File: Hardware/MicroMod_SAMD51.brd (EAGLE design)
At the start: 22 x 22 mm, 36 parts, among them J2 MICROMOD-2222, U1 W25QXX128MBIT-6X5-NO_CENTER, U2 ATSAMD51J20A-A, Y1 32.768kHz

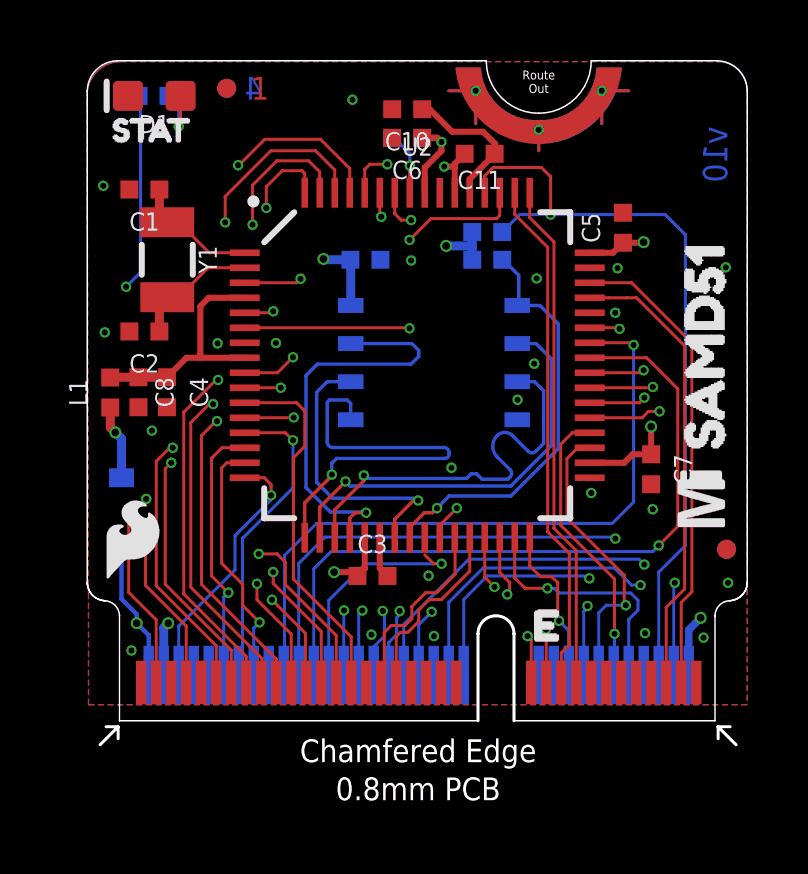
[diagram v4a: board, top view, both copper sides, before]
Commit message: Various testing elements in Variant files regarding Serial1 and Serial2
* Changes old SPI naming convention to new one
* Moves some pins around for more thought out layout (more details to come)
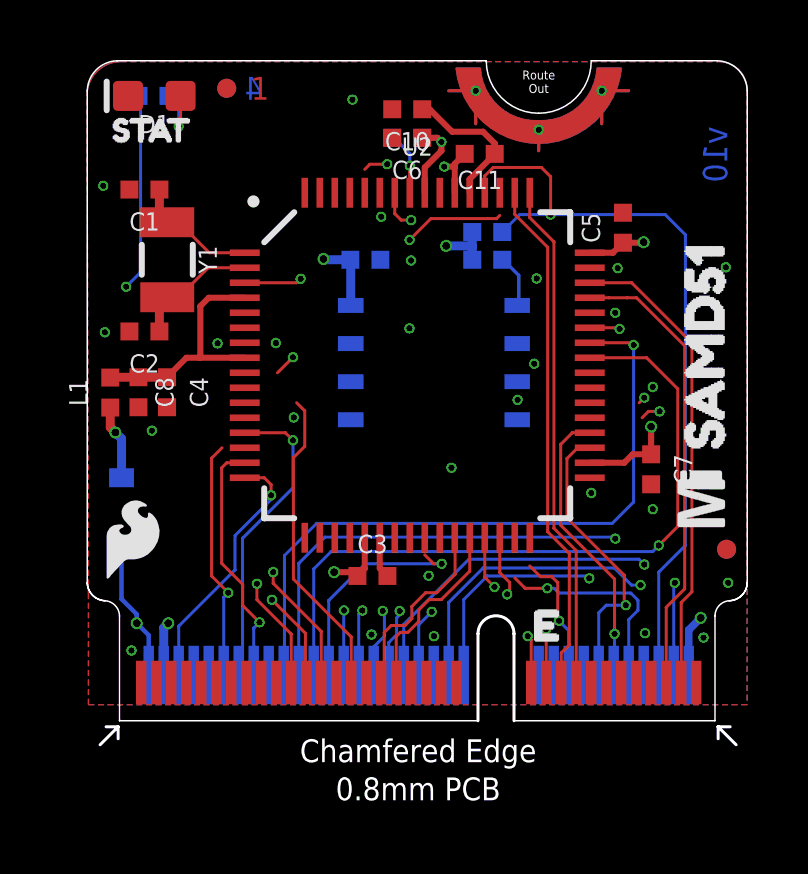
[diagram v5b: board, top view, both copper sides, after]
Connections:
- net MOSI renamed COPI
- net QSPI_DAT1 renamed COPI1
- removed net !CS1: J2.49, U2.64
- removed net A5: J2.65, U2.5
- removed net A6: J2.63, U2.10
- removed net D2: J2.40, U2.37
- removed net D3: J2.42, U2.38
- removed net D4: J2.44, U2.51
- removed net D5: J2.46, U2.60
- removed net D6: J2.48, U2.59
- removed net D7: J2.73, U2.40
- removed net D8/!INT: J2.16, J2.69, U2.26
- removed net MISO: J2.64, U2.14
- removed net MISO1: J2.61, U2.62
- removed net MOSI1: J2.59, U2.61
- removed net QSPI_CS: R4.1, U1.1, U2.24
- removed net QSPI_DAT0: U1.5, U2.17
- removed net QSPI_DAT2: U1.3, U2.19
- removed net QSPI_DAT3: U1.7, U2.20
- removed net QSPI_SCK: U1.6, U2.23
- removed net SCL1: J2.55, U2.29
- removed net SDA1: J2.53, U2.30
- new net !CS1!: R4.1, U1.1
- new net !HOLD!: U1.7
- new net !WP!: U1.3
- new net CIPO: J2.64, U2.15
- new net CIPO1: U2.19
- new net CIPO1\: U1.5
- new net CS1: U2.20
- new net D2/G0: J2.40, U2.9
- new net D3/G1: J2.42, U2.10
- new net D4/G2: J2.44, U2.11
- new net D5/G3: J2.46, U2.12
- new net D6/G4: J2.48, U2.23
- new net D7/G5: J2.73, U2.24
- new net D8/G6: J2.71, U2.25
- new net D9/G7: J2.69, U2.26
- new net HOST_ENABLE: U2.51
- new net I2S_MCLK: J2.58, U2.40
- new net SCL1/TX2: J2.22, J2.55, U2.29
- new net SDA1/RX2: J2.20, J2.53, U2.30
- net 3.3V_EN: no longer U2.39
- net A1: now also U2.61; no longer U2.6
- net A2/PWM0: now also U2.62; no longer U2.12
- net A3/PWM1: now also U2.63; no longer U2.11
- net A4: now also U2.64; no longer U2.9
- net D0: now also U2.5; no longer U2.31
- net D1: now also U2.6; no longer U2.32
- net I2S_CLK: now also U2.39; no longer U2.25
- net SCLK: now also U2.14; no longer U2.15
- net SCLK1: now also U1.6, U2.17; no longer J2.57, U2.63
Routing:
- net D7: track 27.9 -> 0.00 mm, vias 2 -> 0
- net D8/!INT: track 25.5 -> 0.00 mm, vias 3 -> 0
- net MOSI1: track 24.3 -> 0.00 mm, vias 2 -> 0
- net MISO1: track 23.1 -> 0.00 mm, vias 2 -> 0
- net SCLK1: track 22.0 -> 0.00 mm, vias 2 -> 0
- net !CS1: track 20.7 -> 0.00 mm, vias 2 -> 0
- net D5: track 19.2 -> 0.00 mm, vias 2 -> 0
- net D4: track 19.2 -> 0.00 mm, vias 2 -> 0
- net D2: track 18.7 -> 0.00 mm, vias 2 -> 0
- net D3: track 18.6 -> 0.00 mm, vias 3 -> 0
- net D5/G3: track 0.00 -> 18.4 mm, vias 0 -> 2
- net D4/G2: track 0.00 -> 18.4 mm, vias 0 -> 2
- net A5: track 17.2 -> 0.00 mm, vias 2 -> 0
- net D2/G0: track 0.00 -> 17.0 mm, vias 0 -> 2
- net D3/G1: track 0.00 -> 16.9 mm, vias 0 -> 3
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
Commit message: Begins routing, removes old
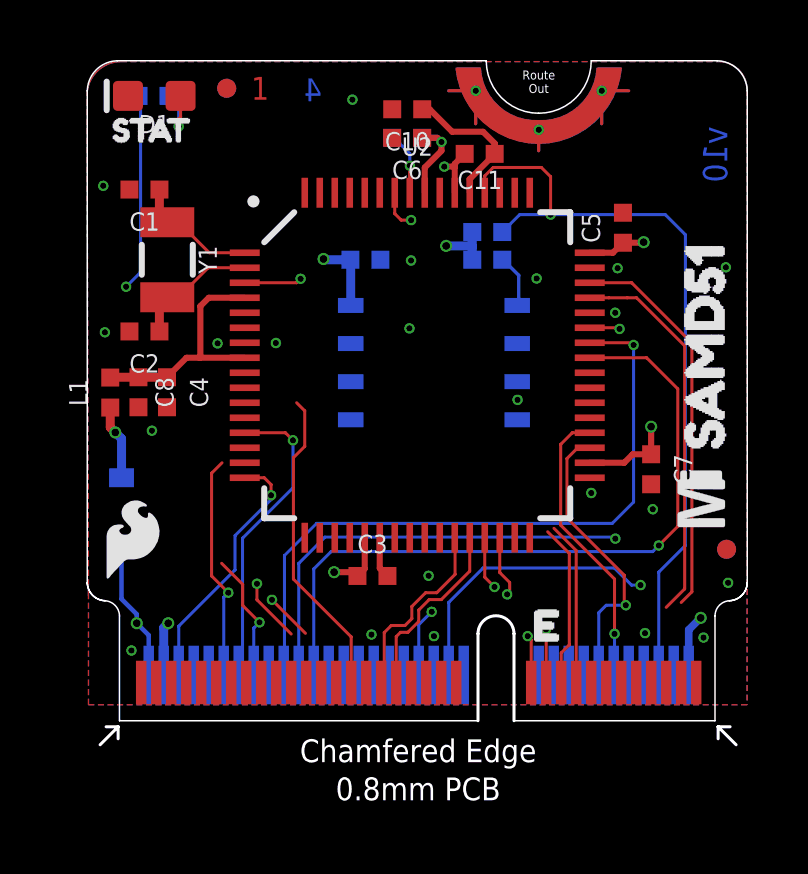
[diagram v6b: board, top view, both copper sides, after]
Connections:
- net D+ renamed D+/USB_HOST_D+
- net D- renamed D-/USBHOST_D-
- net I2S_WS renamed I2S_FS
- removed net CIPO1\: U1.5
- removed net CS1: U2.20
- new net D10: J2.67, U2.31
- new net D11: J2.65, U2.32
- new net I2C_!INT!: J2.16, U2.37
- net !CS1!: now also U2.20
- net !HOLD!: now also U2.50
- net !WP!: now also U2.49
- net 3.3V_EN: now also U2.38
- net A4: now also J2.49; no longer J2.51
- net CIPO1: now also U1.5
- net HOST_ENABLE: now also J2.8
- net RXI: now also U2.59; no longer U2.50
- net SCL1/TX2: now also J2.53; no longer J2.55
- net SDA1/RX2: now also J2.51; no longer J2.53
- net TXO: now also U2.60; no longer U2.49
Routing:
- net A2/PWM0: track 24.0 -> 0.00 mm, vias 3 -> 0
- net D5/G3: track 18.4 -> 0.00 mm, vias 2 -> 0
- net D4/G2: track 18.4 -> 0.00 mm, vias 2 -> 0
- net D2/G0: track 17.0 -> 0.00 mm, vias 2 -> 0
- net D3/G1: track 16.9 -> 0.00 mm, vias 3 -> 0
- net D6/G4: track 15.9 -> 0.00 mm, vias 2 -> 0
- net A4: track 13.5 -> 0.00 mm, vias 2 -> 0
- net RXI: track 17.2 -> 5.44 mm
- net TXO: track 17.0 -> 5.45 mm
- net 3.3V_EN: track 10.0 -> 0.00 mm, vias 2 -> 0
- net I2S_CLK: track 7.44 -> 0.00 mm, vias 1 -> 0
- net D0: track 7.03 -> 0.00 mm, vias 1 -> 0
- net D1: track 4.39 -> 0.00 mm, vias 1 -> 0
- net SCLK: track 8.34 -> 4.33 mm
- net D+/USB_HOST_D+: track 15.7 -> 13.0 mm
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
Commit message: Adds routing to all but a few lines
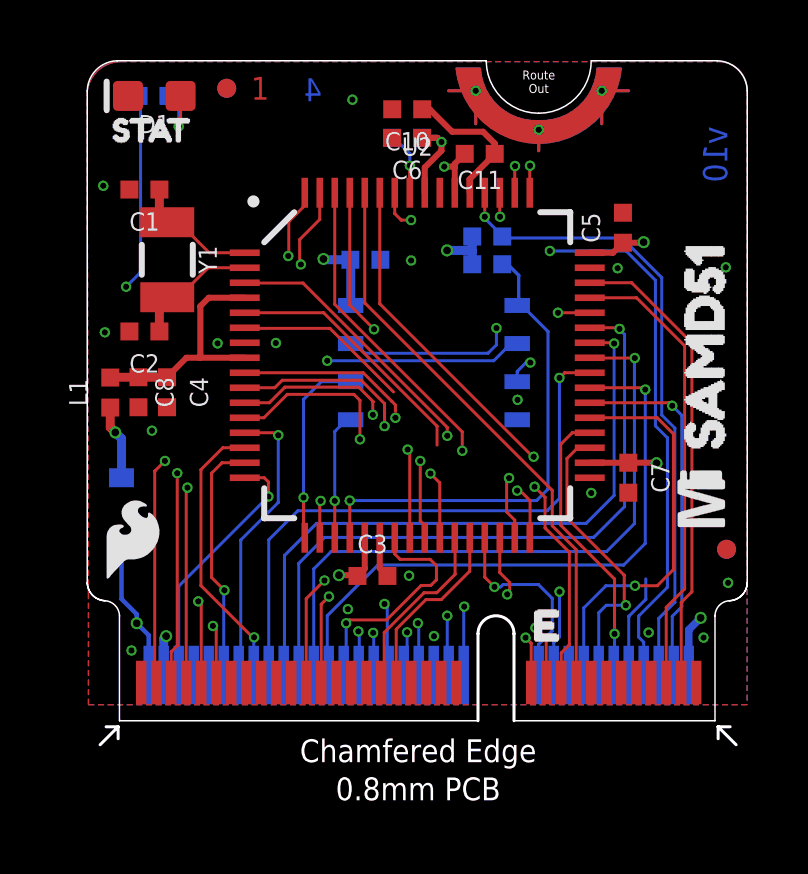
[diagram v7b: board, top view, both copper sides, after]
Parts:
- moved C7 0.81 mm to (18.0, 8.10)
- moved R1 0.15 mm to (13.3, 16.1)
- moved R4 0.15 mm to (13.3, 15.2)
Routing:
- net HOST_ENABLE: track 0.00 -> 21.1 mm, vias 0 -> 2
- net I2S_CLK: track 0.00 -> 20.6 mm, vias 0 -> 1
- net I2S_MCLK: track 0.00 -> 19.9 mm, vias 0 -> 1
- net D10: track 0.00 -> 19.1 mm, vias 0 -> 2
- net D7/G5: track 0.00 -> 18.8 mm, vias 0 -> 2
- net D8/G6: track 0.00 -> 18.1 mm, vias 0 -> 2
- net D11: track 0.00 -> 18.1 mm, vias 0 -> 2
- net A2/PWM0: track 0.00 -> 17.9 mm, vias 0 -> 2
- net D9/G7: track 0.00 -> 17.1 mm, vias 0 -> 2
- net D2/G0: track 0.00 -> 14.7 mm, vias 0 -> 2
- net !CS1!: track 1.79 -> 16.4 mm, vias 0 -> 1
- net A0: track 31.3 -> 17.0 mm, vias 3 -> 2
- net D3/G1: track 0.00 -> 14.2 mm, vias 0 -> 2
- net D4/G2: track 0.00 -> 13.8 mm, vias 0 -> 2
- net TXO: track 5.45 -> 19.2 mm
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
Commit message: Finishing routing, and fixes minor DRC errors regarding wire stubs
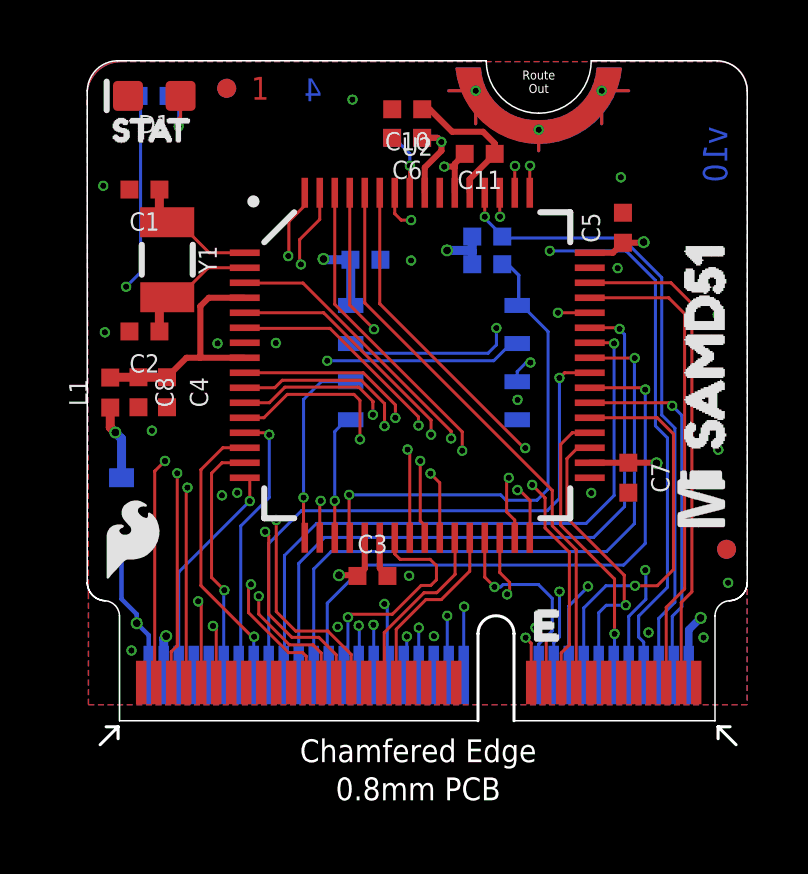
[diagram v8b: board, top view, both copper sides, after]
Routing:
- net D1: track 5.85 -> 20.2 mm, vias 0 -> 2
- net D0: track 12.0 -> 21.4 mm, vias 0 -> 2
- net A4: track 11.2 -> 18.4 mm, vias 1 -> 2
- net A3/PWM1: track 12.6 -> 18.6 mm, vias 1 -> 2
- net SDA1/RX2: track 15.7 -> 19.3 mm
- net SCL1/TX2: track 16.1 -> 19.2 mm
- net !CS: track 8.52 -> 7.72 mm
- net D+/USB_HOST_D+: track 15.7 -> 16.5 mm
- net D-/USBHOST_D-: track 15.3 -> 15.9 mm
- net D10: track 19.1 -> 19.0 mm, vias 2 -> 3
- net GND: vias 19 -> 21
- net D11: vias 2 -> 3
